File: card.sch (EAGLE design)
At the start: 56 parts, among them IC3 LTC1992CMS8, IC4 LTC1992CMS8, SW1 SPST_TACT-EVQQ2, SW2 SPST_TACT-EVQQ2, SW3 SPST_TACT-EVQQ2, SW4 SPST_TACT-EVQQ2

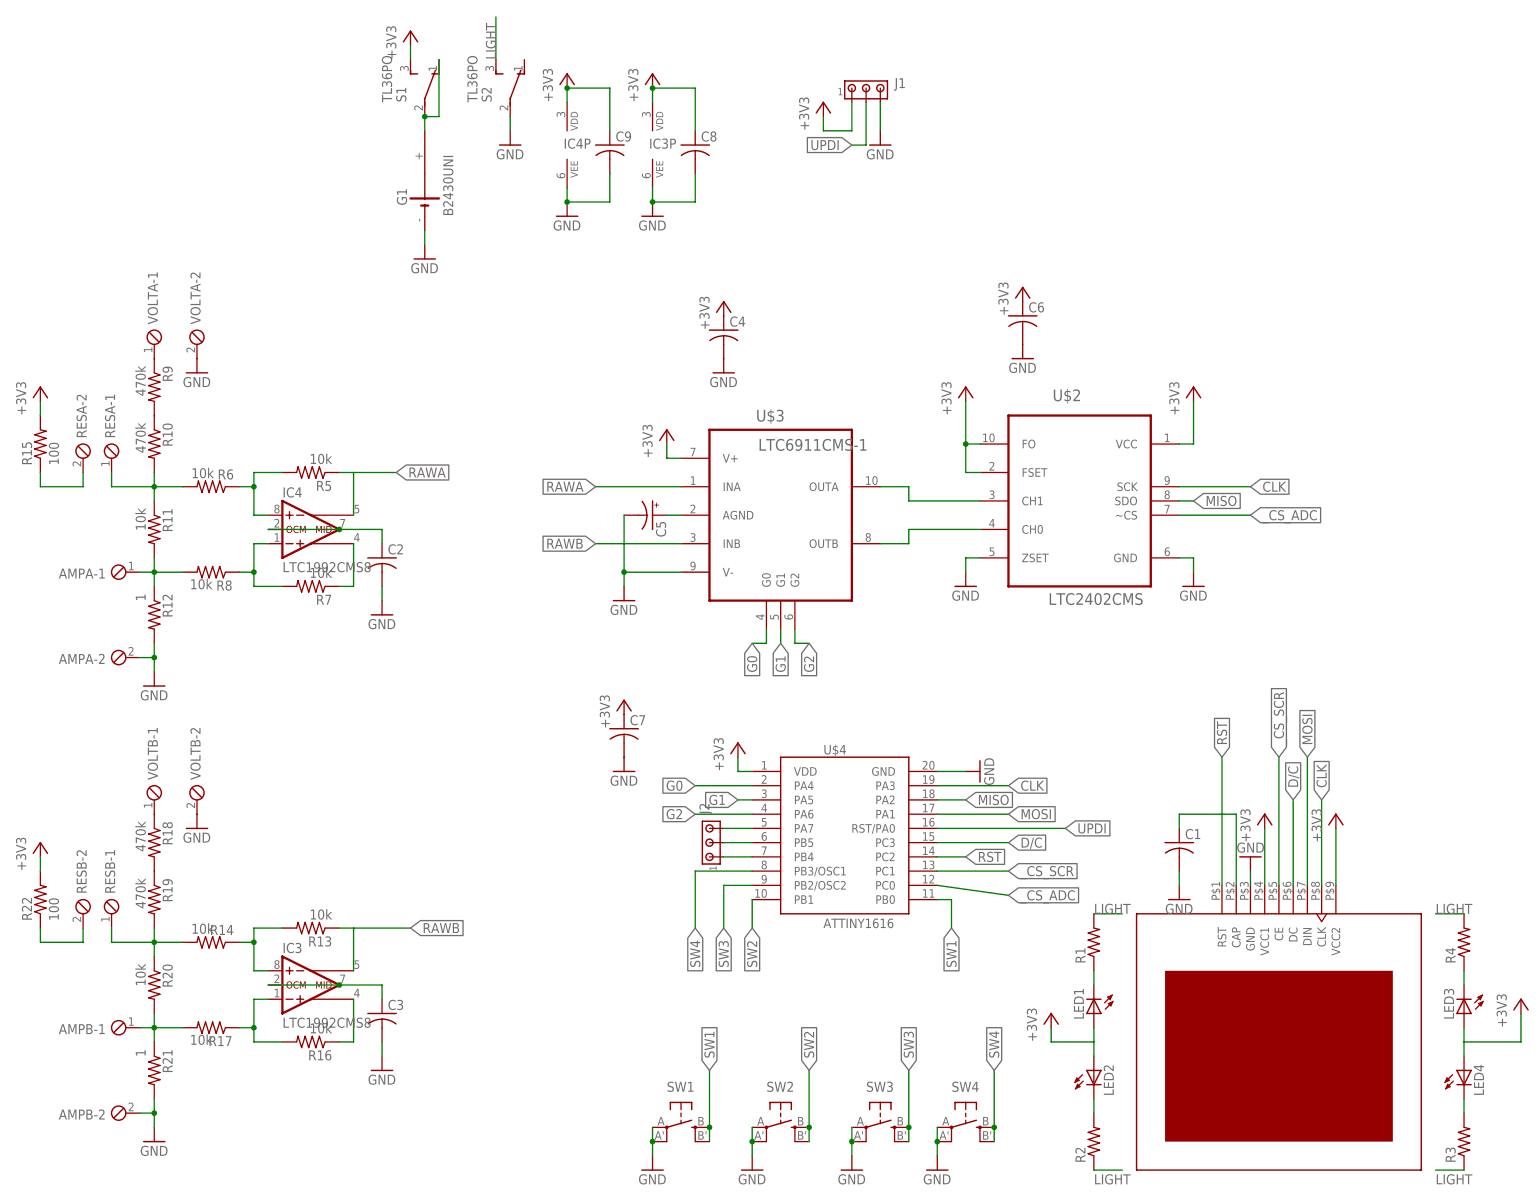
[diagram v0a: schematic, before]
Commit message: Added components values
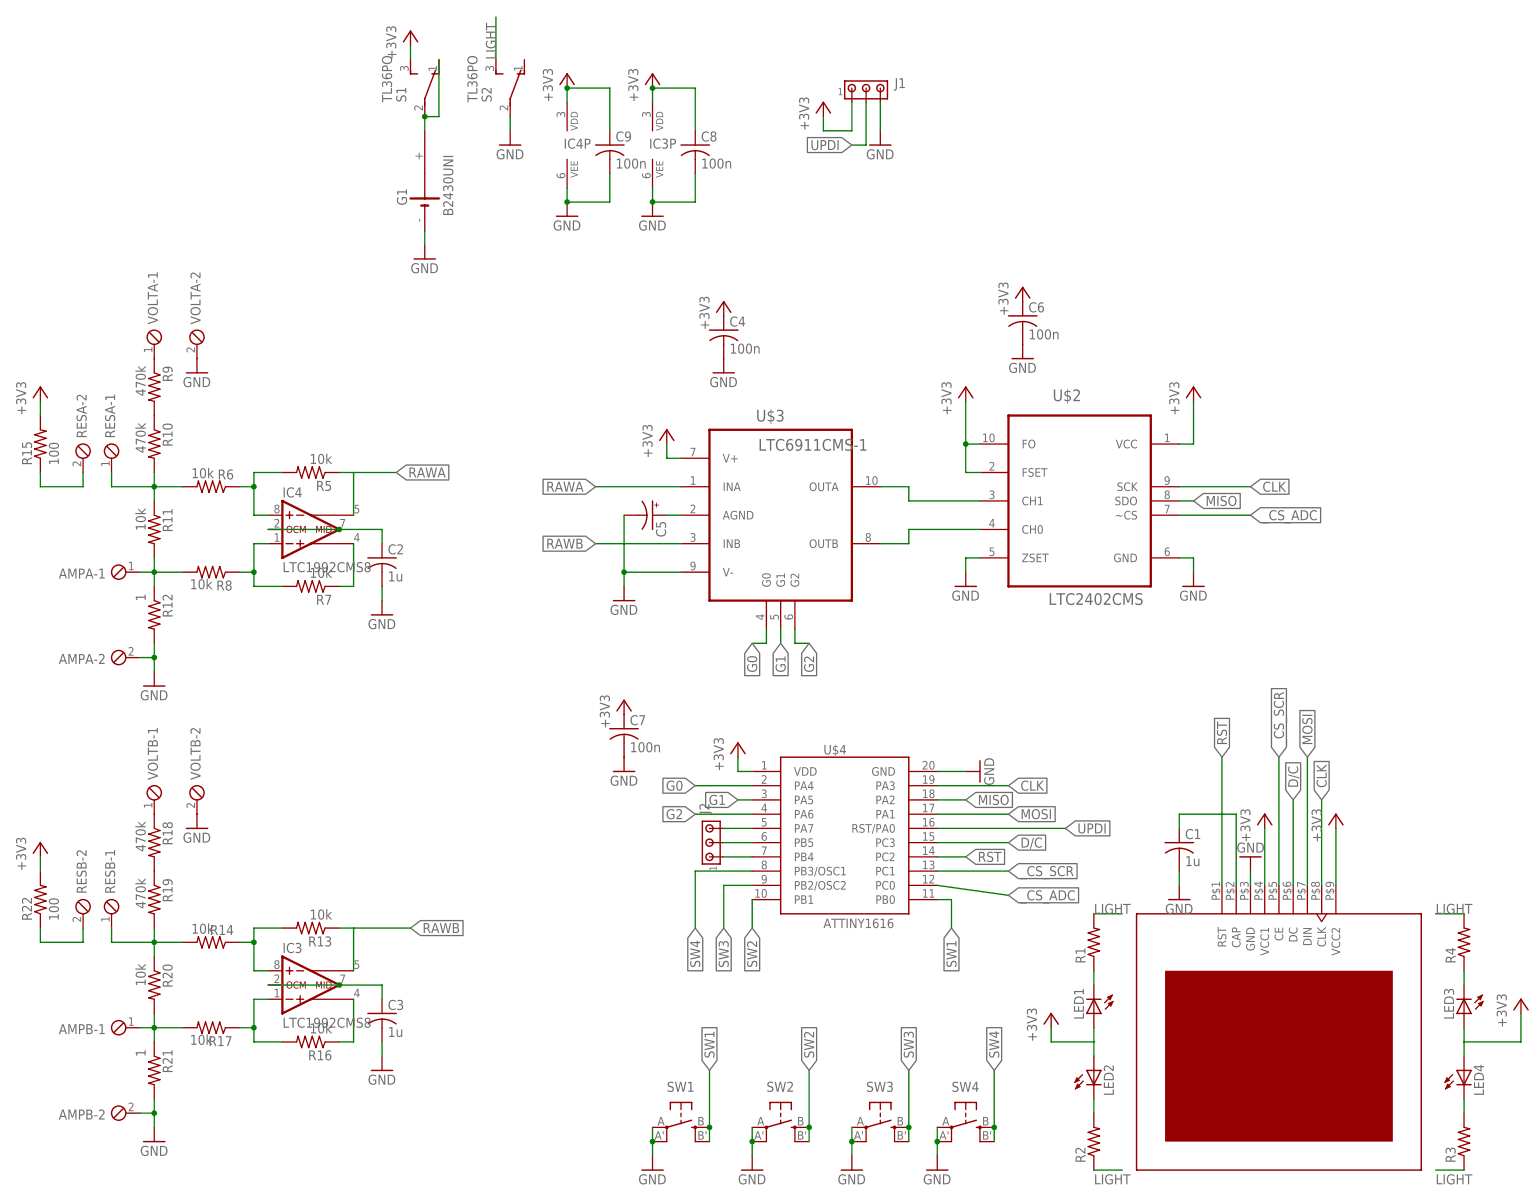
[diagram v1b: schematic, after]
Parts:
- C1, C2, C3: value (none) -> 1u
- C4, C6, C7, C8, C9: value (none) -> 100n
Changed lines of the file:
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@@
 <part name="R3" library="resistor" deviceset="R-US_" device="M0805"/>
 <part name="R4" library="resistor" deviceset="R-US_" device="M0805"/>
-<part name="C1" library="resistor" deviceset="C-US" device="C0805"/>
+<part name="C1" library="resistor" deviceset="C-US" device="C0805" value="1u"/>
 <part name="G1" library="battery" deviceset="B2430UNI" device=""/>
 <part name="SW1" library="adafruit" deviceset="SPST_TACT" device="-EVQQ2"/>
@@
 <part name="R7" library="resistor" deviceset="R-US_" device="M0805" value="10k"/>
 <part name="R8" library="resistor" deviceset="R-US_" device="M0805" value="10k"/>
-<part name="C2" library="resistor" deviceset="C-US" device="C0805"/>
+<part name="C2" library="resistor" deviceset="C-US" device="C0805" value="1u"/>
 <part name="GND5" library="supply1" deviceset="GND" device=""/>
 <part name="GND11" library="supply1" deviceset="GND" device=""/>
@@
 <part name="R16" library="resistor" deviceset="R-US_" device="M0805" value="10k"/>
 <part name="R17" library="resistor" deviceset="R-US_" device="M0805" value="10k"/>
-<part name="C3" library="resistor" deviceset="C-US" device="C0805"/>
+<part name="C3" library="resistor" deviceset="C-US" device="C0805" value="1u"/>
 <part name="GND15" library="supply1" deviceset="GND" device=""/>
 <part name="R18" library="resistor" deviceset="R-US_" device="M0805" value="470k"/>
@@
 <part name="GND18" library="supply1" deviceset="GND" device=""/>
 <part name="C5" library="adafruit" deviceset="CPOL-US" device="A/3216-18R"/>
-<part name="C4" library="adafruit" deviceset="C-US" device="C0805K"/>
-<part name="C6" library="adafruit" deviceset="C-US" device="C0805K"/>
-<part name="C7" library="adafruit" deviceset="C-US" device="C0805K"/>
+<part name="C4" library="adafruit" deviceset="C-US" device="C0805K" value="100n"/>
+<part name="C6" library="adafruit" deviceset="C-US" device="C0805K" value="100n"/>
+<part name="C7" library="adafruit" deviceset="C-US" device="C0805K" value="100n"/>
 <part name="+3V12" library="supply1" deviceset="+3V3" device=""/>
 <part name="GND19" library="supply1" deviceset="GND" device=""/>
@@
 <part name="+3V16" library="supply1" deviceset="+3V3" device=""/>
 <part name="GND23" library="supply1" deviceset="GND" device=""/>
-<part name="C8" library="adafruit" deviceset="C-US" device="C0805K"/>
-<part name="C9" library="adafruit" deviceset="C-US" device="C0805K"/>
+<part name="C8" library="adafruit" deviceset="C-US" device="C0805K" value="100n"/>
+<part name="C9" library="adafruit" deviceset="C-US" device="C0805K" value="100n"/>
 <part name="+3V7" library="supply1" deviceset="+3V3" device=""/>
 <part name="+3V8" library="supply1" deviceset="+3V3" device=""/>

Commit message: Updated design and curved traces
Ready to ship !
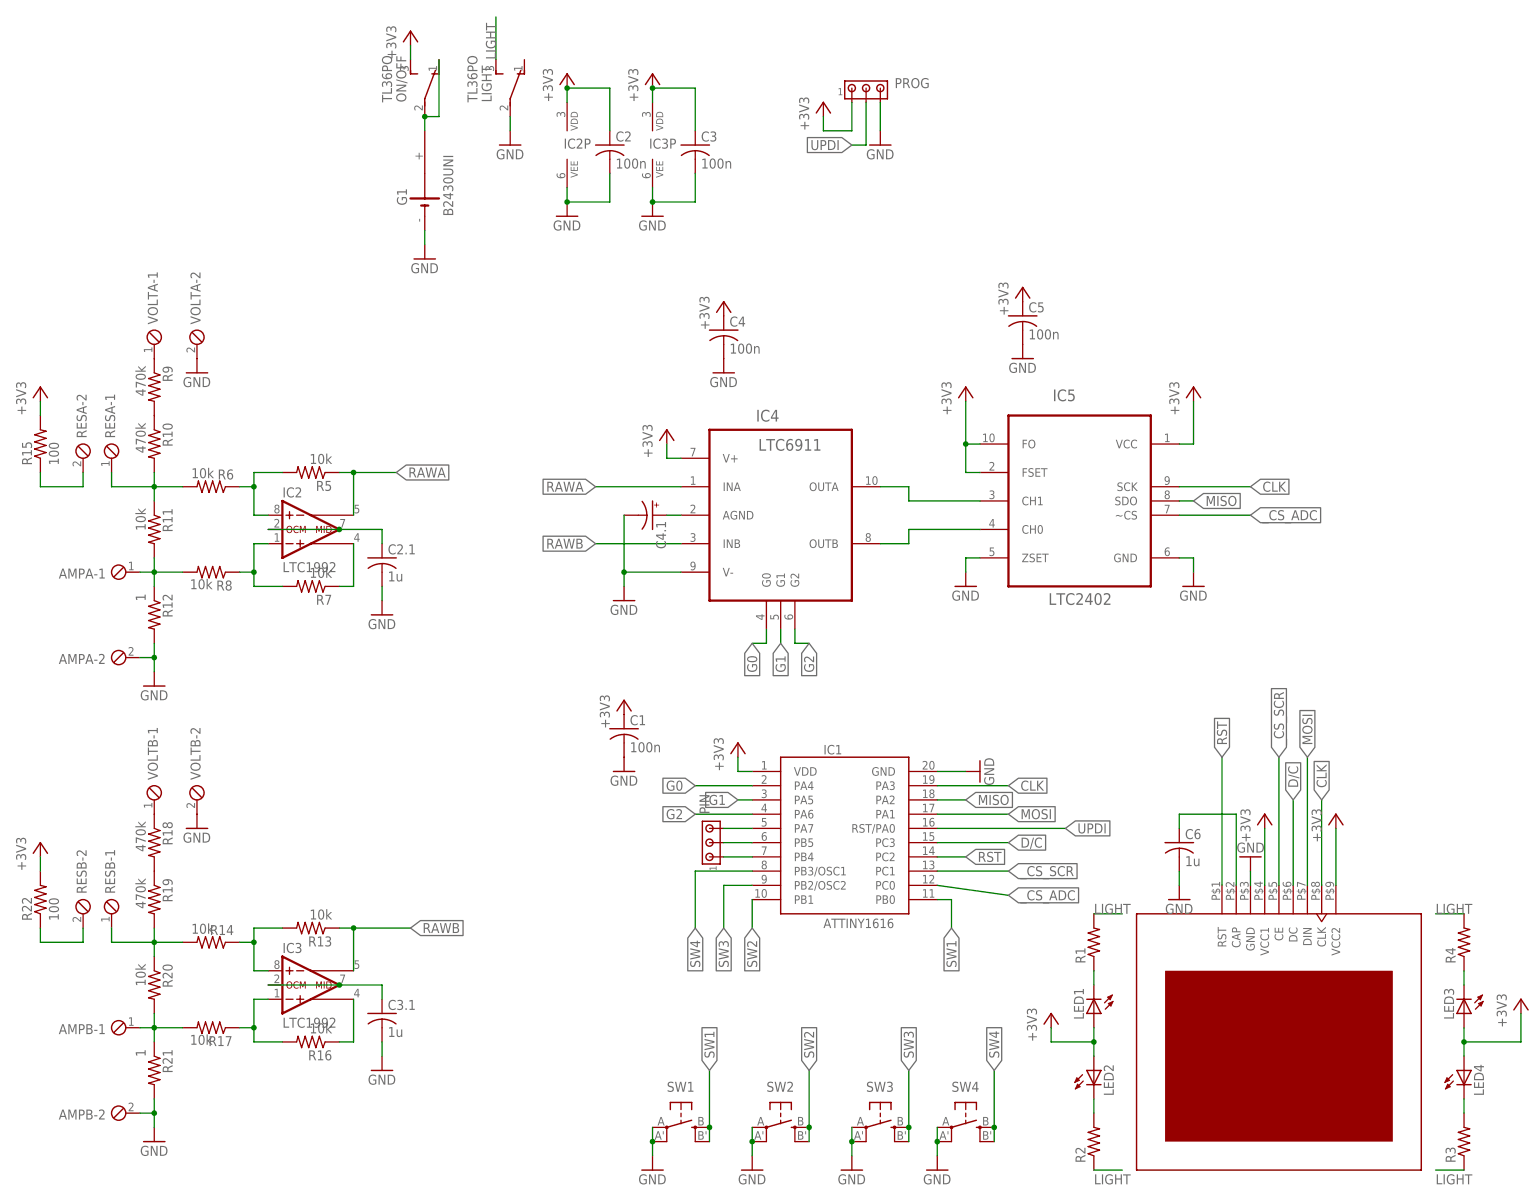
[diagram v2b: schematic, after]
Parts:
- removed C7, C8, C9: 100n, adafruit:C-USC0805K
- removed U$3: LTC6911CMS-1, HomeMade:LTC6911CMS-1
- added C2.1, C3.1: 1u, resistor:C-USC0805
- added C4.1: (no value), adafruit:CPOL-USA/3216-18R
- added IC2: LTC1992, linear-technology-2:LTC1992CMS8
- C1, C2, C3: value 1u -> 100n; device resistor:C-USC0805 -> adafruit:C-USC0805K
- C5: value (none) -> 100n; device adafruit:CPOL-USA/3216-18R -> adafruit:C-USC0805K
- C6: value 100n -> 1u; device adafruit:C-USC0805K -> resistor:C-USC0805
- IC3: value LTC1992CMS8 -> LTC1992
- IC4: value LTC1992CMS8 -> LTC6911; device linear-technology-2:LTC1992CMS8 -> HomeMade:LTC6911CMS-1
- IC5: value LTC2402CMS -> LTC2402
- renumbered J1 to PROG, J2 to PIN, S1 to ON/OFF, S2 to LIGHT, U$2 to IC5, U$4 to IC1
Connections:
- net +3V3: now also C1.1, C2.1, C3.1, C5.1, IC2P.VDD, IC4.V+; no longer C6.1, C7.1, C8.1, C9.1, IC4P.VDD, U$3.V+
- net G0: now also IC4.G0; no longer U$3.G0
- net G1: now also IC4.G1; no longer U$3.G1
- net G2: now also IC4.G2; no longer U$3.G2
- net GND: now also C2.1.2, C3.1.2, C4.1.-, C5.2, IC2P.VEE, IC4.V-; no longer C5.-, C7.2, C8.2, C9.2, IC4P.VEE, U$3.V-
- net N$16: now also IC2G$1.-IN; no longer IC4G$1.-IN
- net N$17: now also IC2G$1.+IN; no longer IC4G$1.+IN
- net N$18: now also C4.1.+, IC4.AGND; no longer C5.+, U$3.AGND
- net N$19: now also IC2G$1.+OUT; no longer IC4G$1.+OUT
- net N$21: now also C2.1.1, IC2G$1.MID, IC2G$1.OCM; no longer C2.1, IC4G$1.MID, IC4G$1.OCM
- net N$29: now also IC4.OUTB; no longer U$3.OUTB
- net N$3: now also C6.1; no longer C1.1
- net N$31: now also C3.1.1; no longer C3.1
- net N$37: now also IC4.OUTA; no longer U$3.OUTA
- net RAWA: now also IC2G$1.-OUT, IC4.INA; no longer IC4G$1.-OUT, U$3.INA
- net RAWB: now also IC4.INB; no longer U$3.INB
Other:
- moved on the sheet: C1, C2, C3, C6

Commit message: Few changes, added logo
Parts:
- removed R10, R9: 470k, resistor:R-US_M0805
- added R34: 1, resistor:R-US_M0805
- added R39: 100, resistor:R-US_M0805
- C4.1: value (none) -> 1u
- R21: value 1 -> 470k
- R22: value 100 -> 470k
- R61, R62, R63, R64: value (none) -> 330
- renumbered R1 to R61, R11 to R23, R12 to R24, R13 to R36, R14 to R35, R15 to R29, R16 to R38, R17 to R37, R18 to R31, R19 to R32, R2 to R62, R20 to R33, R3 to R64, R4 to R63, R5 to R26, R6 to R25, R7 to R28, R8 to R27
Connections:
- net +3V3: now also R39.2; no longer R22.2
- net GND: now also R34.2; no longer R21.2
- net N$22: now also R21.2, R22.1; no longer R10.1, R9.2
- net N$23: now also R22.2; no longer R10.2
- net N$27: now also R21.1; no longer R9.1
- net N$34: now also R34.1; no longer R21.1
- net N$36: now also R39.1; no longer R22.1
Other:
- moved on the sheet: R21, R22
